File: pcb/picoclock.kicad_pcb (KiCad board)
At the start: 2 copper layers, 175.8 x 64 mm, 88 parts, among them J1 UART, J10 USB, J11 Alt Power, J12 LED_5V, J15 Conn_01x24, J3 xx, J4 xx, J5 Micro_SD_Card_Det1, J6 USB_C_Receptacle, J7 xx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

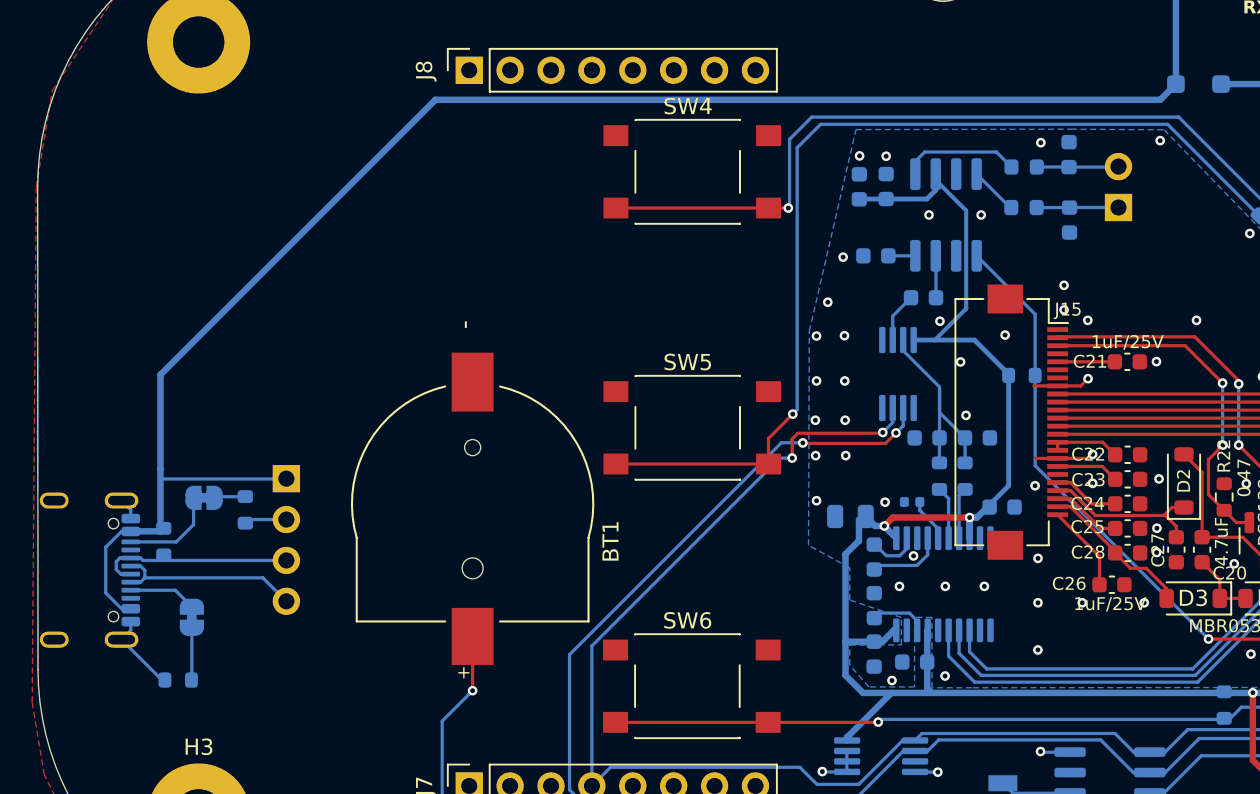
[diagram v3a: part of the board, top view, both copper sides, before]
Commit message: [pcb] add USB-A
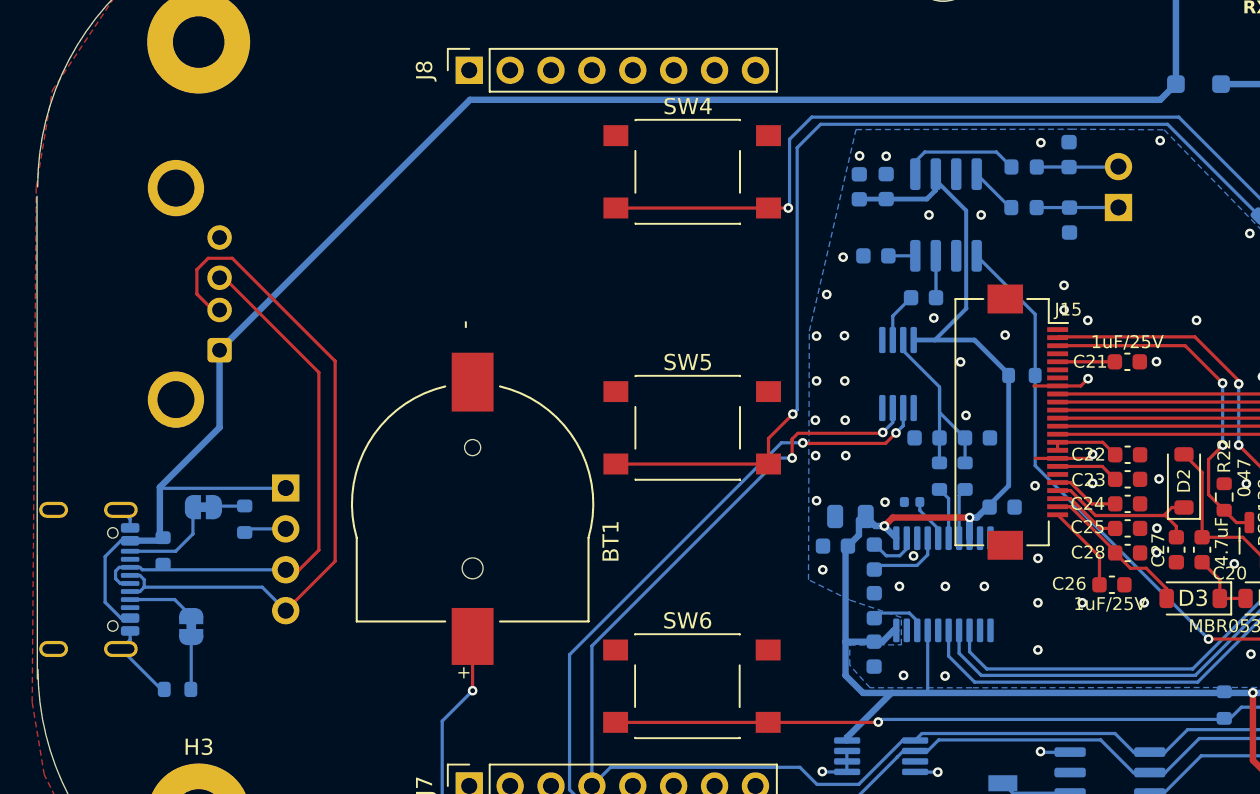
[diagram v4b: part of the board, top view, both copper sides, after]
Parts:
- added J2: USB_A, Connector_USB:USB_A_Connfly_DS1095, B.Cu at (70.2, 94.0)
- moved C4 8.72 mm to (108.5, 106.2)
- moved J10 0.58 mm to (74.3, 102.6)
- moved R5 0.58 mm to (71.8, 104.5)
- moved R6 0.58 mm to (67.6, 115.1)
- moved J6 0.58 mm to (61.0, 108.3)
- moved JP1 0.58 mm to (68.4, 111.2)
- moved JP2 0.58 mm to (69.2, 103.8)
- moved R7 0.58 mm to (66.7, 106.5)
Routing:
- net USB D-: track 11.8 -> 43.0 mm
- net USB D+: track 12.2 -> 34.4 mm
- net LED_5V+: track 192.0 -> 191.3 mm
- net GND: vias 75 -> 76
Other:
- outline, holes or cut-outs redrawn

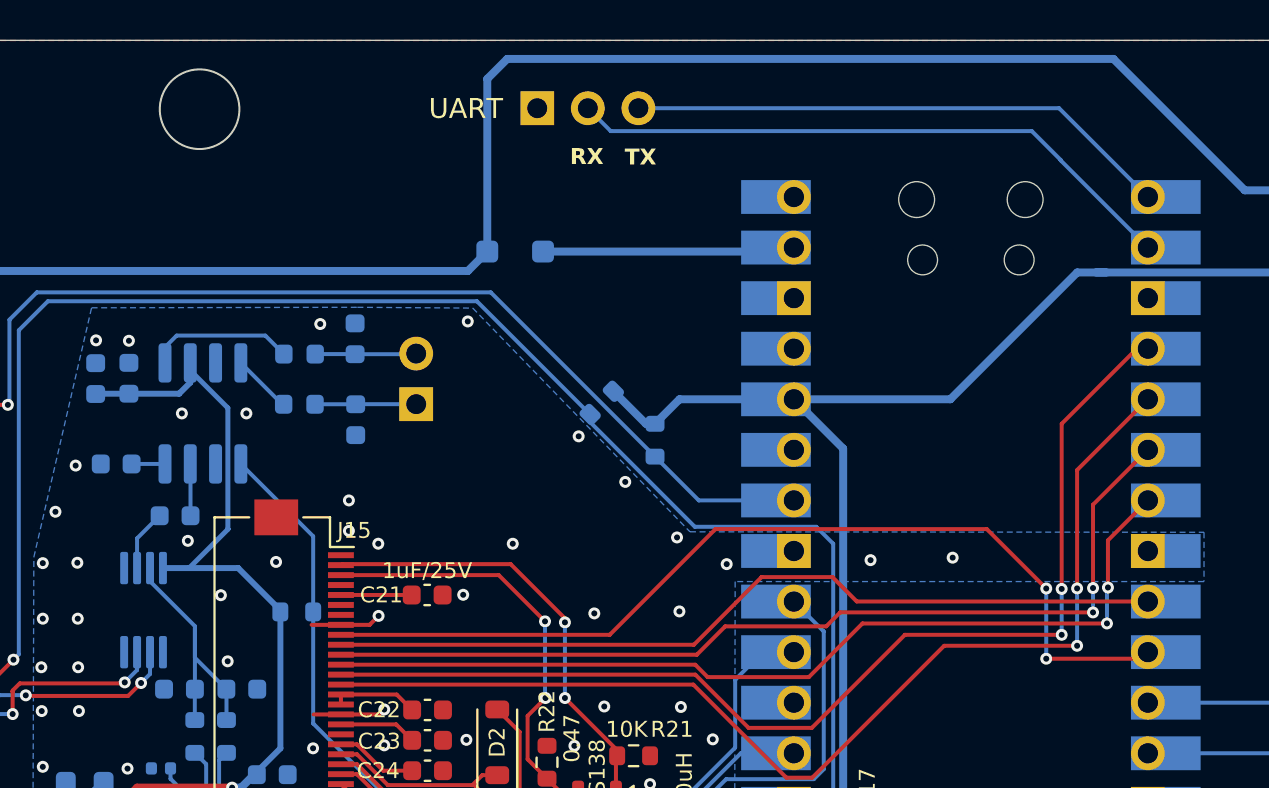
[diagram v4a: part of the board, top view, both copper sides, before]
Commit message: [pcb] move symbols into common lib, add pogo pins on pico
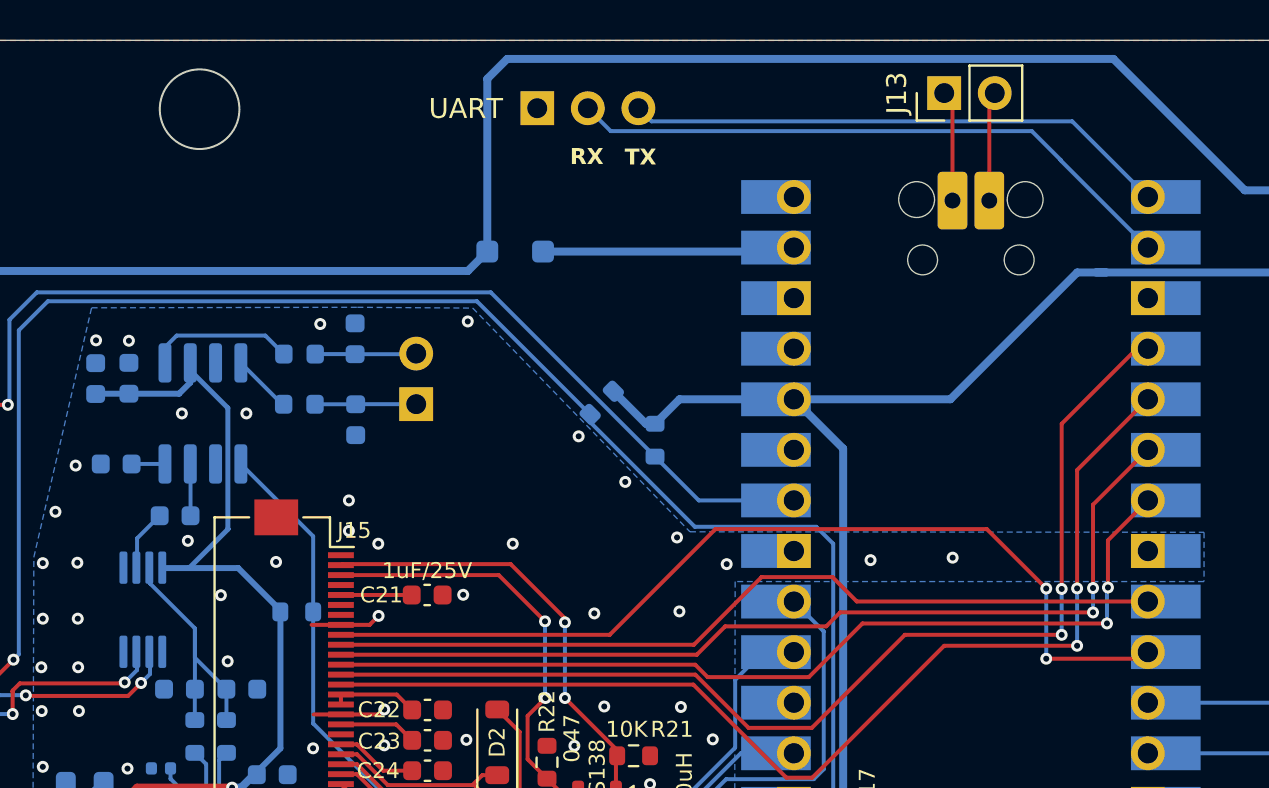
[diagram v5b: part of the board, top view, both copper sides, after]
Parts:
- added J13: USB_PICO, Connector_PinHeader_2.54mm:PinHeader_1x02_P2.54mm_Vertical, F.Cu at (152.6, 69.5)
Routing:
- net Net-(J13-Pin_1): track 0.00 -> 5.57 mm
- net Net-(J13-Pin_2): track 0.00 -> 5.51 mm

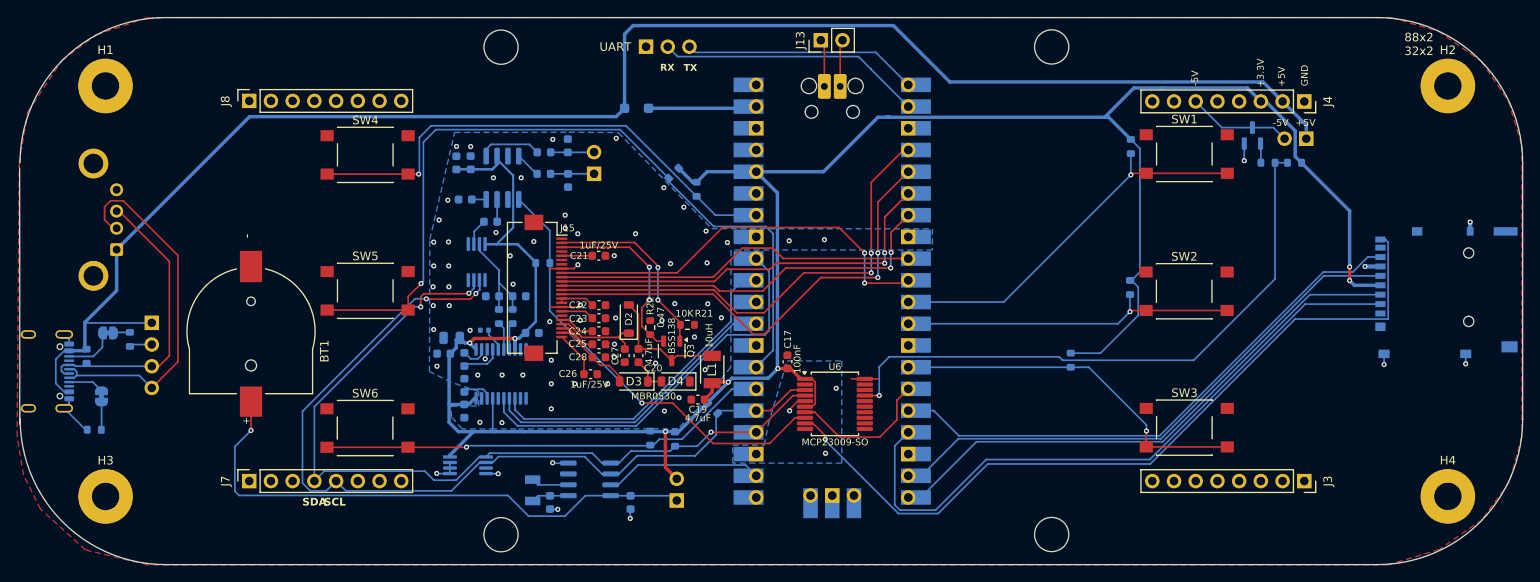
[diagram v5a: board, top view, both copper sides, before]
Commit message: [pcb] adjust pcb outline
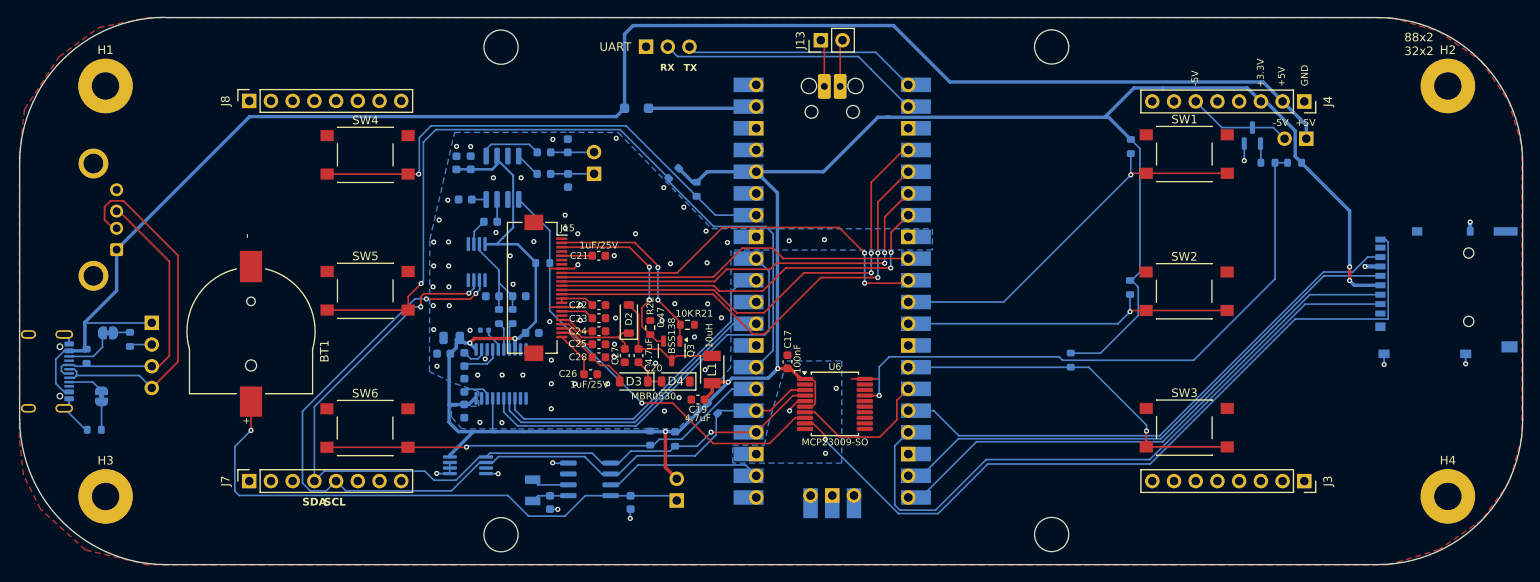
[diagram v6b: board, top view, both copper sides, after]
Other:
- outline, holes or cut-outs redrawn
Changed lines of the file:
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@@
 	)
 	(gr_line
-		(start 217.64 130.869185)
-		(end 75.910815 130.869185)
+		(start 217.64 130.87)
+		(end 75.91 130.87)
 		(stroke
 			(width 0.05)
-			(type default)
+			(type solid)
 		)
 		(layer "Edge.Cuts")
 	)
 	(gr_arc
-		(start 75.910815 130.869185)
-		(mid 63.89 125.89)
-		(end 58.910815 113.869185)
+		(start 75.910815 130.87)
+		(mid 63.890001 125.890812)
+		(end 58.85 113.87)
 		(stroke
 			(width 0.05)
-			(type default)
+			(type solid)
 		)
 		(layer "Edge.Cuts")
@@
 	)
 	(gr_line
-		(start 234.64 83.89)
-		(end 234.64 113.869185)
+		(start 234.64 83.9)
+		(end 234.64 113.87)
 		(stroke
 			(width 0.05)
-			(type default)
+			(type solid)
 		)
 		(layer "Edge.Cuts")
@@
 	)
 	(gr_line
-		(start 58.85 84.47)
-		(end 58.870815 114.449185)
+		(start 58.85 83.9)
+		(end 58.85 113.87)
 		(stroke
 			(width 0.05)
-			(type default)
+			(type solid)
 		)
 		(layer "Edge.Cuts")
 	)
 	(gr_arc
-		(start 58.89 83.89)
-		(mid 63.869185 71.869185)
-		(end 75.89 66.89)
+		(start 58.85 83.89)
+		(mid 63.847972 71.843829)
+		(end 75.9 66.86)
 		(stroke
 			(width 0.05)
-			(type default)
+			(type solid)
 		)
 		(layer "Edge.Cuts")
@@
 		(start 217.64 66.89)
 		(mid 229.660815 71.869185)
-		(end 234.64 83.89)
+		(end 234.64 83.9)
 		(stroke
 			(width 0.05)
-			(type default)
+			(type solid)
 		)
 		(layer "Edge.Cuts")
@@
 	)
 	(gr_arc
-		(start 234.64 113.869185)
+		(start 234.64 113.87)
 		(mid 229.660815 125.89)
-		(end 217.64 130.869185)
+		(end 217.64 130.87)
 		(stroke
 			(width 0.05)
-			(type default)
+			(type solid)
 		)
 		(layer "Edge.Cuts")
@@
 				(xy 73.8 66.9) (xy 219.3 66.9) (xy 224.8 68.5) (xy 229.8 72) (xy 233 76.7) (xy 234.55 81.9) (xy 234.55 115.9)
 				(xy 233.1 121.2) (xy 229.9 125.6) (xy 224.9 129.1) (xy 218.9 130.9) (xy 73.8 130.9) (xy 66.55 129.15)
-				(xy 61.3 124.4) (xy 59.3 120.4) (xy 58.55 115.9) (xy 58.8 83.9) (xy 59.8 77.9) (xy 63.8 71.9) (xy 67.8 68.9)
+				(xy 61.3 124.4) (xy 59.3 120.4) (xy 58.82 116.11) (xy 58.83 82.78) (xy 59.42 77.62) (xy 63.45 71.48)
+				(xy 68.09 68.07)
 			)
 		)
